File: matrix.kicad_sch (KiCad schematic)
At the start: 126 parts, among them SW10 8, SW11 9, SW12 0, SW13 - _, SW14 = +, SW15 \ |, SW17 Tab, SW18 Q, SW19 W, SW2 Esc, SW20 E, SW21 R, SW22 T, SW23 Y, SW24 U, SW25 I, SW26 O, SW27 P, SW28 { [, SW29 } ], SW3 1, SW30 Del, SW31 Ctrl, SW32 A, SW33 S, SW34 D, SW35 F, SW36 G, SW37 H, SW38 J, SW39 K, SW4 2, SW40 L, SW41 ; :, SW42 ' ", SW43 Return, SW44 Shift, SW45 Z, SW46 X, SW47 C, SW48 V, SW49 B, SW5 3, SW50 N, SW51 M, SW52 , <, SW53 . >, SW54 / ?, SW55 Shift, SW56 Fn, SW57 Option, SW58 Super, SW59 Space, SW6 4, SW60 Super, SW61 Option, SW62 Left Mouse, SW63 Middle Mouse, SW64 Right Mouse, SW7 5, SW8 6, SW9 7

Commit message: schema mostly done with footprints added
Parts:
- D1, D10, D11, D12, D13, D14, D15, D16, D17, D18, D19, D2, D20, D21, D22, D23, D24, D25, D26, D27, D28, D29, D3, D30, D31, D32, D33, D34, D35, D36, D37, D38, D39, D4, D40, D41, D42, D43, D44, D45, D46, D47, D48, D49, D5, D50, D51, D52, D53, D54, D55, D56, D57, D58, D59, D6, D60, D61, D62, D63, D7, D8, D9: footprint (none) -> Diode_SMD:D_SOD-123
- SW10, SW11, SW12, SW13, SW14, SW15, SW16, SW18, SW19, SW2, SW20, SW21, SW22, SW23, SW24, SW25, SW26, SW27, SW28, SW29, SW3, SW32, SW33, SW34, SW35, SW36, SW37, SW38, SW39, SW4, SW40, SW41, SW42, SW45, SW46, SW47, SW48, SW49, SW5, SW50, SW51, SW52, SW53, SW54, SW56, SW57, SW6, SW61, SW7, SW8, SW9: footprint (none) -> MX_Only:MXOnly-1U
- SW17, SW30, SW58, SW60: footprint (none) -> MX_Only:MXOnly-1.5U
- SW31, SW55: footprint (none) -> MX_Only:MXOnly-1.75U
- SW43, SW44: footprint (none) -> MX_Only:MXOnly-2.25U
- SW59: footprint (none) -> MX_Only:MXOnly-6U
- SW62, SW64: footprint (none) -> Kalih Choc:KailhChoc-1.5U
- SW63: footprint (none) -> Kalih Choc:KailhChoc-1U

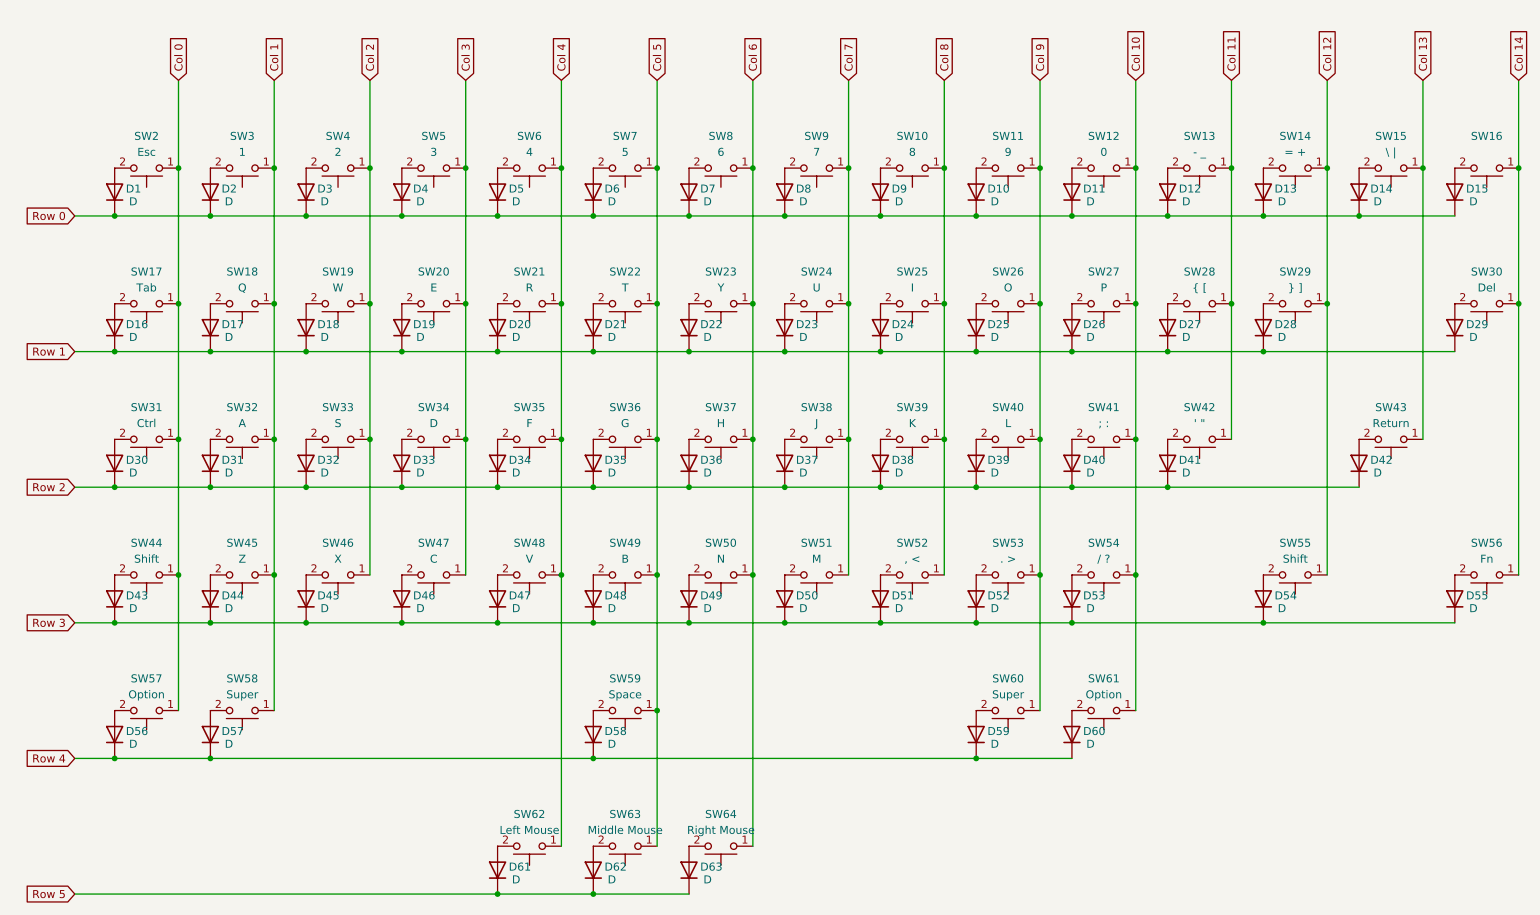
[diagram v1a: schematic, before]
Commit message: pcb finished except for routing
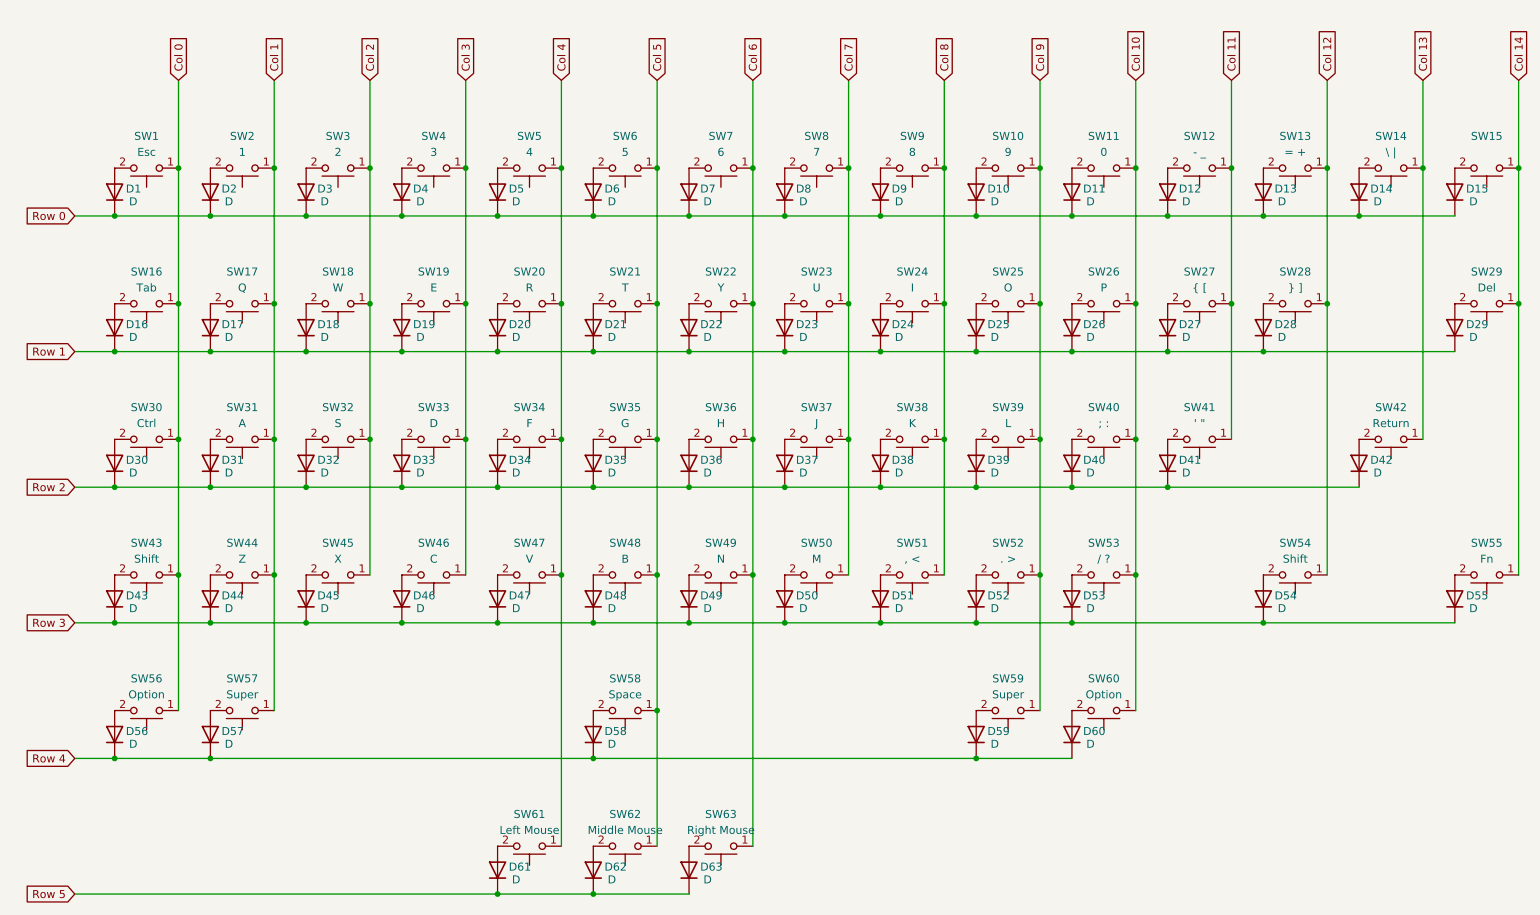
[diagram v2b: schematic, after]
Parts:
- renumbered SW2 to SW1, SW11 to SW10, SW12 to SW11, SW13 to SW12, SW14 to SW13, SW15 to SW14, SW16 to SW15, SW17 to SW16, SW18 to SW17, SW19 to SW18, SW20 to SW19, SW3 to SW2, SW21 to SW20, SW22 to SW21, SW23 to SW22, SW24 to SW23, SW25 to SW24, SW26 to SW25, SW27 to SW26, SW28 to SW27, SW29 to SW28, SW30 to SW29, SW4 to SW3, SW31 to SW30, SW32 to SW31, SW33 to SW32, SW34 to SW33, SW35 to SW34, SW36 to SW35, SW37 to SW36, SW38 to SW37, SW39 to SW38, SW40 to SW39, SW5 to SW4, SW41 to SW40, SW42 to SW41, SW43 to SW42, SW44 to SW43, SW45 to SW44, SW46 to SW45, SW47 to SW46, SW48 to SW47, SW49 to SW48, SW50 to SW49, SW6 to SW5, SW51 to SW50, SW52 to SW51, SW53 to SW52, SW54 to SW53, SW55 to SW54, SW56 to SW55, SW57 to SW56, SW58 to SW57, SW59 to SW58, SW60 to SW59, SW7 to SW6, SW61 to SW60, SW62 to SW61, SW63 to SW62, SW64 to SW63, SW8 to SW7, SW9 to SW8, SW10 to SW9

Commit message: more revisions
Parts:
- SW43: footprint MX_Only:MXOnly-2.25U -> MX_Only:MXOnly-2.25U-ReversedStabilizers-NoLED
- SW58: footprint MX_Only:MXOnly-6U -> MX_Only:MXOnly-6U-ReversedStabilizers-NoLED
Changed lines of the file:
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@@
 			)
 		)
-		(property "Footprint" "MX_Only:MXOnly-2.25U"
+		(property "Footprint" "MX_Only:MXOnly-2.25U-ReversedStabilizers-NoLED"
 			(at 36.83 113.03 0)
 			(hide yes)
@@
 			)
 		)
-		(property "Footprint" "MX_Only:MXOnly-6U"
+		(property "Footprint" "MX_Only:MXOnly-6U-ReversedStabilizers-NoLED"
 			(at 113.03 134.62 0)
 			(hide yes)
